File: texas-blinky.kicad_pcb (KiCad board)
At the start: 2 copper layers, 62 x 60.3 mm, 6 parts, among them Q1 MMBT3904

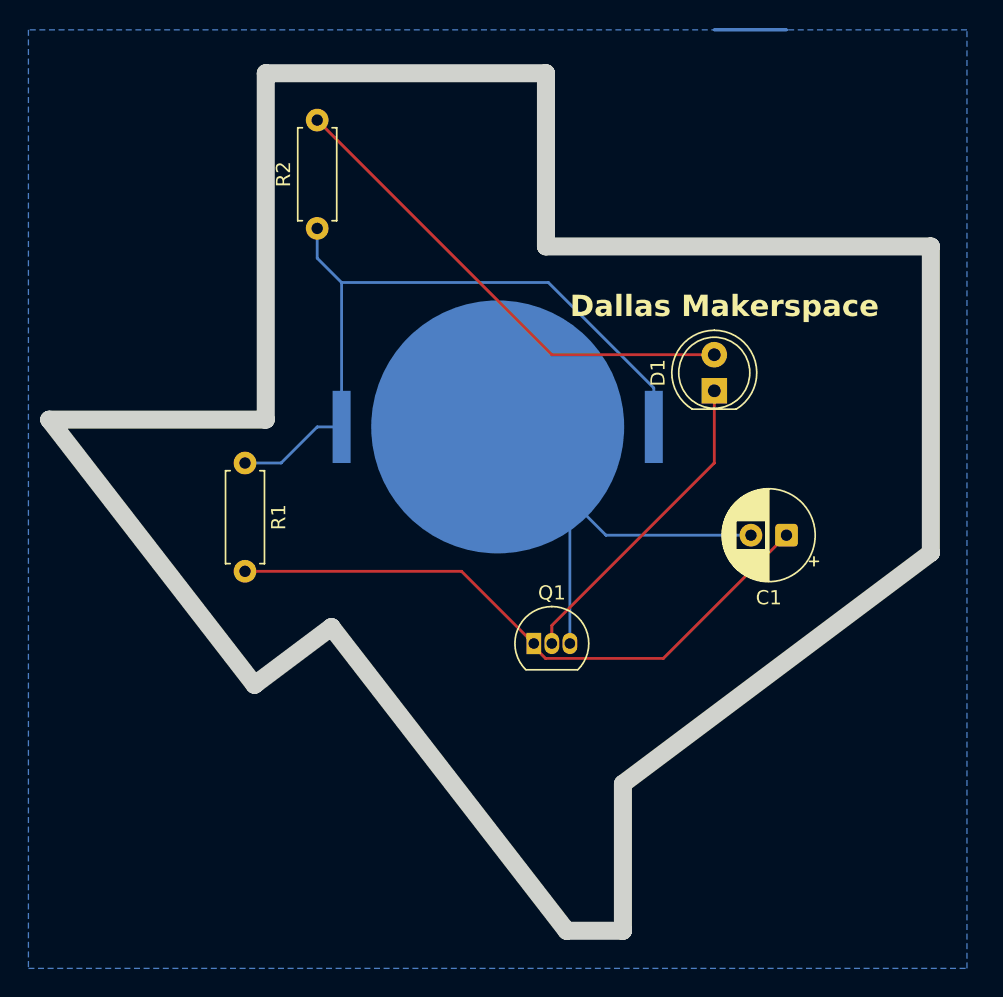
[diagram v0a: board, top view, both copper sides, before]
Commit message: Add J1 power header for external supply
Adds a 2-pin 2.54mm pitch header (J1) in parallel with BT1, allowing
the board to be powered from a bench supply without a CR2032 installed.

Co-Authored-By: Claude Sonnet 4.6 <noreply@anthropic.com>
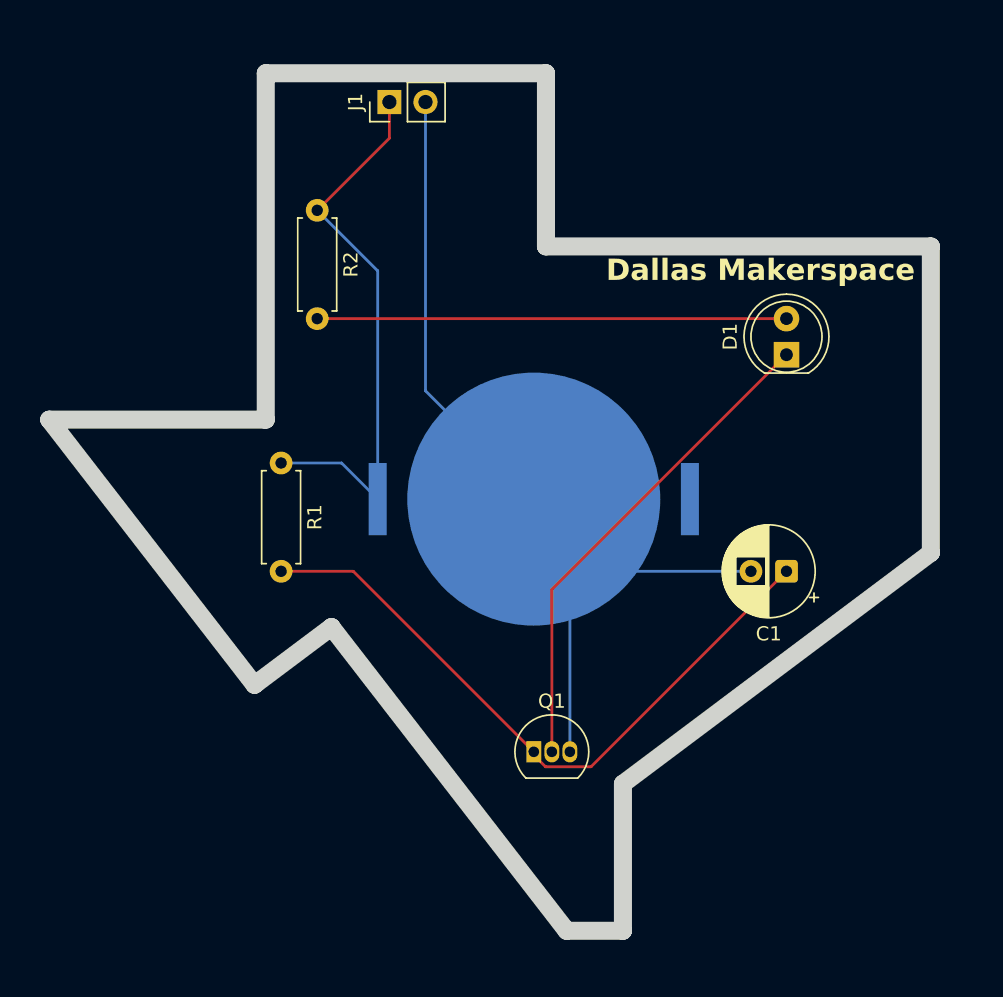
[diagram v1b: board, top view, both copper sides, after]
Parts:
- added J1: Conn_01x02_Pin, Connector_PinHeader_2.54mm:PinHeader_1x02_P2.54mm_Vertical, F.Cu at (119.4, 53.3)
- moved Q1 7.62 mm to (129.5, 99.1)
- moved BT1 5.68 mm to (129.5, 81.3)
- moved D1 5.68 mm to (147.3, 71.1)
- moved C1 2.54 mm to (147.3, 86.4)
- moved R1 2.54 mm to (111.8, 78.7)
- moved R2 1.27 mm to (114.3, 61.0), turned to -90 degrees
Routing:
- net /GND: track 38.3 -> 67.3 mm
- net Net-(D1-K): track 22.5 -> 34.8 mm
- net Net-(BT1-+): track 50.3 -> 39.7 mm
- net Net-(Q1-B): track 44.4 -> 47.1 mm
- net Net-(D1-A): track 34.8 -> 33.0 mm
- removed copper zone on B.Cu, net /GND
